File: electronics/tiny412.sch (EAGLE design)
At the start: 9 parts

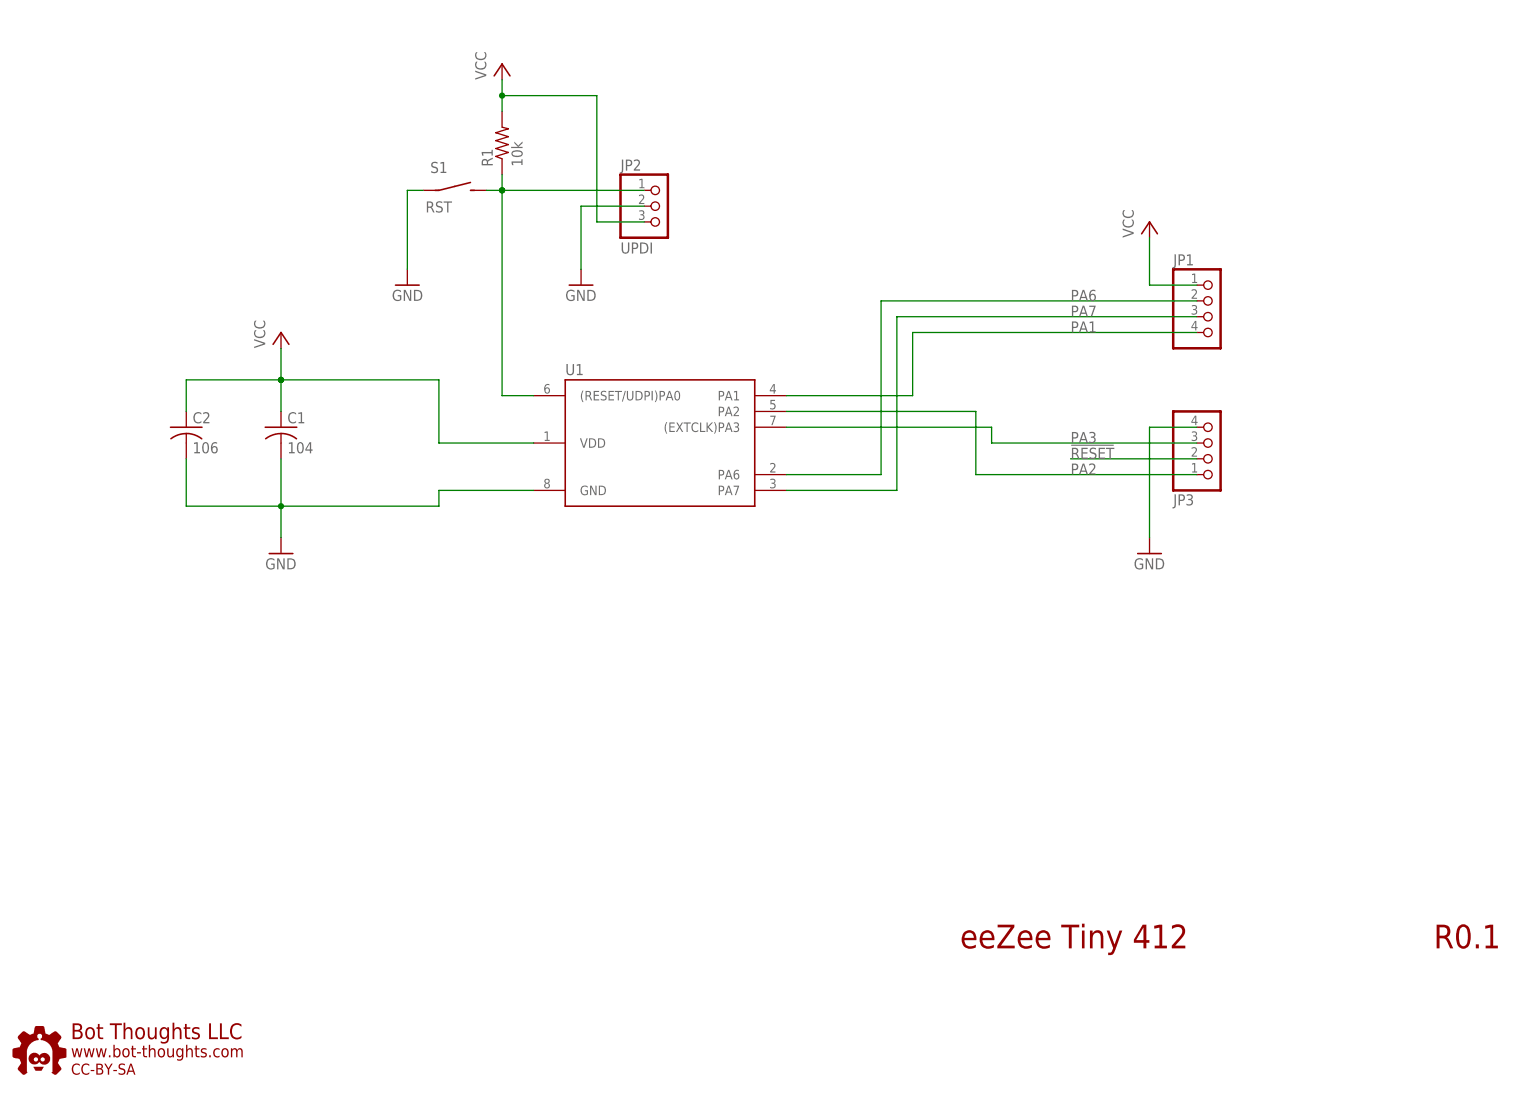
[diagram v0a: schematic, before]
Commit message: Updated silk symbols, enlarged; fixed reset ckt, added HF filter cap
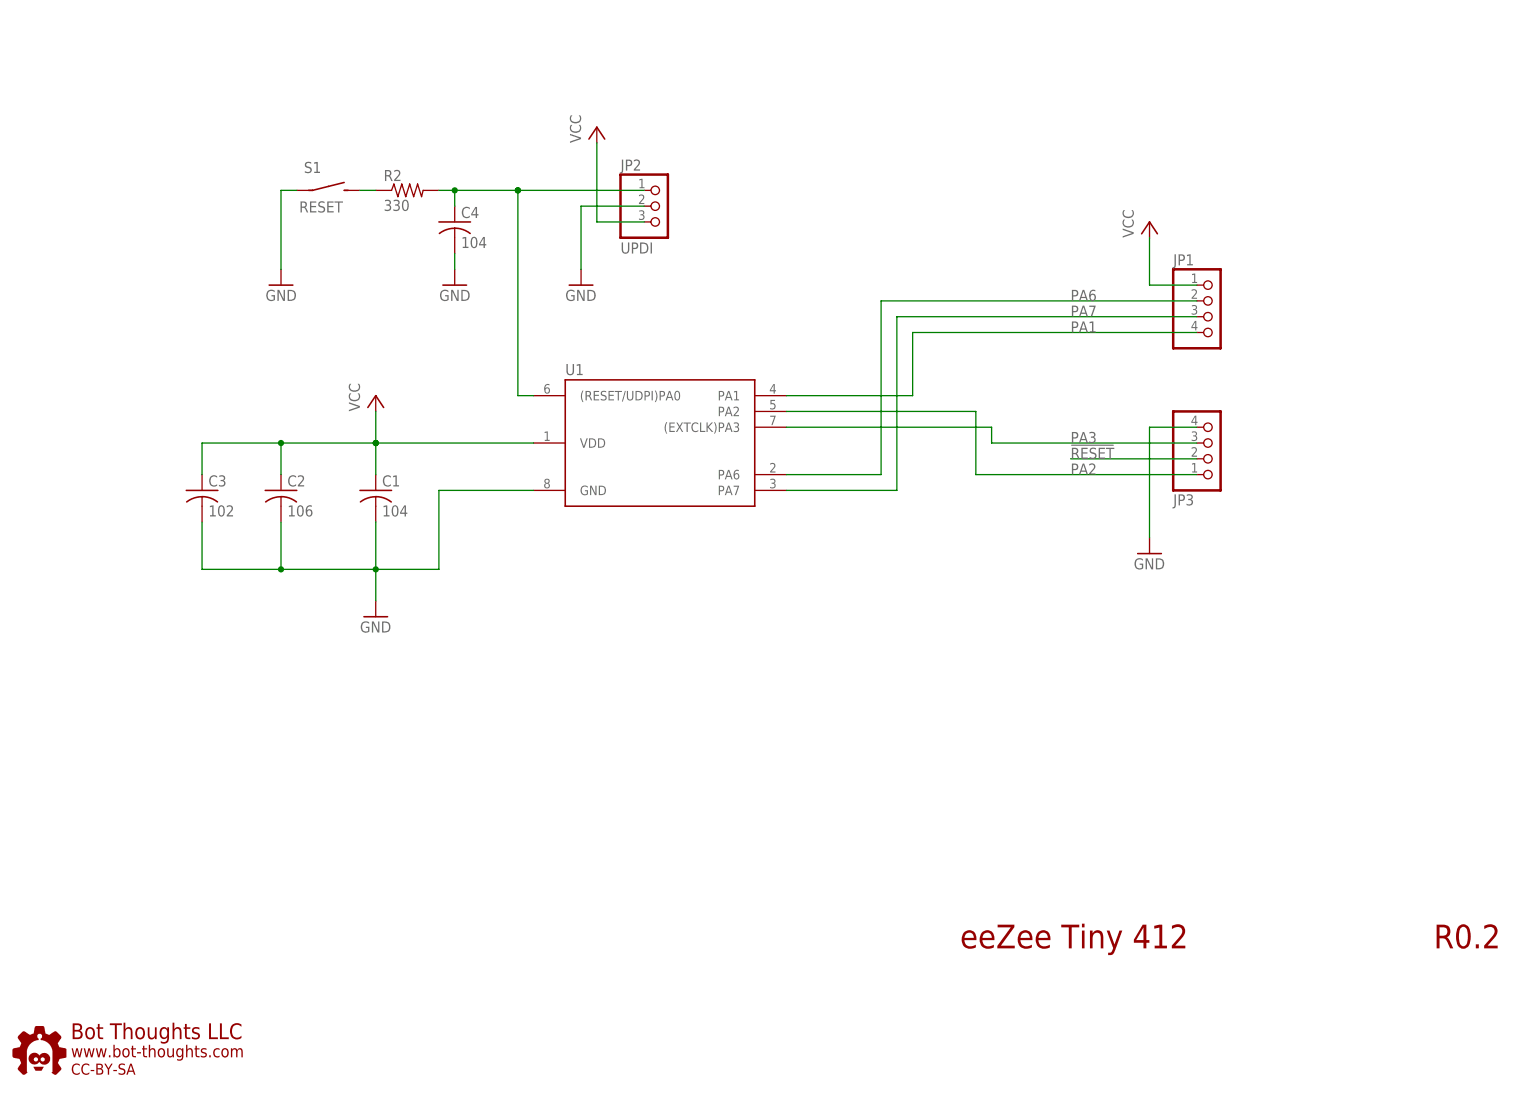
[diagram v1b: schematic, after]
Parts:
- removed R1: 10k, rcl:R-US_R0603
- added C3: 102, rcl:C-USC0603
- added C4: 104, rcl:C-USC0603
- added R2: 330, rcl:R-US_R0603
- C2: device bt_rcl:C-1206 -> bt_rcl:C-0603
- S1: value RST -> RESET
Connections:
- new net N$1: R2.1, S1.S
- net !RESET: now also C4.1, R2.2; no longer R1.1, S1.S
- net GND: now also C3.2, C4.2
- net VCC: now also C3.1; no longer R1.2
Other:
- note added: "R0.2"
- note removed: "R0.1"
- moved on the sheet: C1, C2, S1

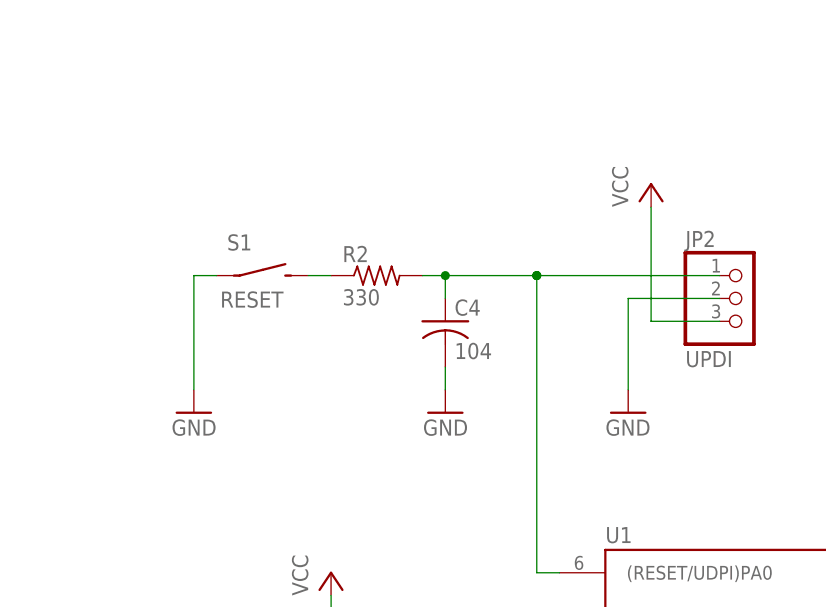
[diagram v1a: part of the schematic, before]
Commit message: remove reset, updated pin desc, added doc url
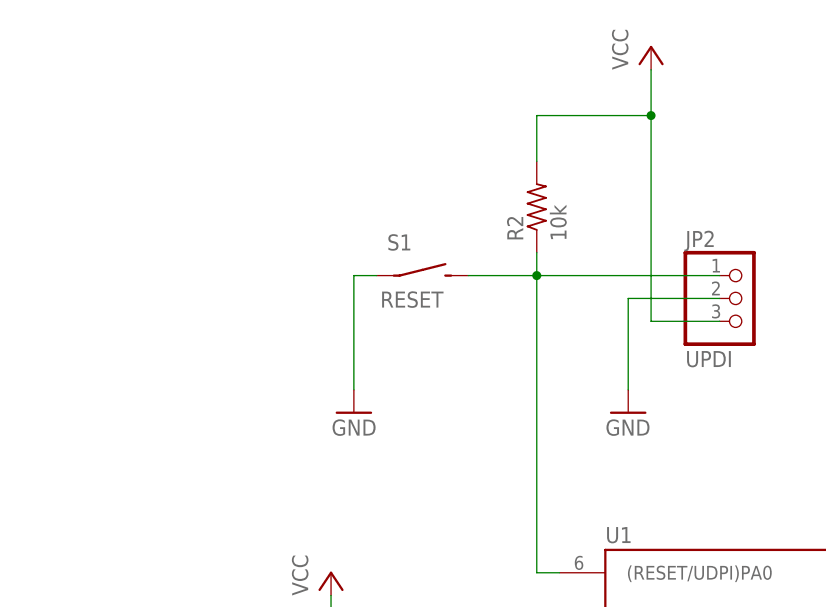
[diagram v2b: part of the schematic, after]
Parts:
- removed C4: 104, rcl:C-USC0603
- R2: value 330 -> 10k
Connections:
- removed net N$1: R2.1, S1.S
- net !RESET: now also R2.1, S1.S; no longer C4.1, R2.2
- net GND: no longer C4.2
- net VCC: now also R2.2
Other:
- moved on the sheet: R2, S1
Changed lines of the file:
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@@
 <attribute name="PARTNO" value="0603YC104KAT2A"/>
 </part>
-<part name="R2" library="rcl" deviceset="R-US_" device="R0603" value="330">
+<part name="R2" library="rcl" deviceset="R-US_" device="R0603" value="10k">
 <attribute name="PARTNO" value="ERJ-3GEYJ103V"/>
 </part>
-<part name="C4" library="rcl" deviceset="C-US" device="C0603" value="104">
-<attribute name="BOM" value="EXCLUDE"/>
-<attribute name="PARTNO" value="0603YC104KAT2A"/>
-</part>
-<part name="GND1" library="supply1" deviceset="GND" device=""/>
 </parts>
 <sheets>
@@
 </plain>
 <instances>
-<instance part="P+1" gate="VCC" x="96.52" y="154.94"/>
+<instance part="P+1" gate="VCC" x="96.52" y="170.18"/>
 <instance part="GND2" gate="1" x="93.98" y="129.54"/>
 <instance part="C1" gate="G$1" x="60.96" y="96.52">
@@
 <attribute name="BOM" value="EXCLUDE" x="60.96" y="96.52" size="1.778" layer="96" display="off"/>
 </instance>
-<instance part="GND3" gate="1" x="45.72" y="129.54" rot="MR0"/>
+<instance part="GND3" gate="1" x="63.5" y="129.54" rot="MR0"/>
 <instance part="P+2" gate="VCC" x="60.96" y="111.76"/>
 <instance part="P+4" gate="VCC" x="185.42" y="139.7"/>
@@
 </instance>
 <instance part="GND4" gate="1" x="185.42" y="86.36"/>
-<instance part="S1" gate="S1" x="53.34" y="144.78"/>
+<instance part="S1" gate="S1" x="71.12" y="144.78"/>
 <instance part="U$1" gate="G$1" x="2.54" y="2.54"/>
 <instance part="JP2" gate="A" x="106.68" y="142.24"/>
@@
 <attribute name="BOM" value="EXCLUDE" x="33.02" y="96.52" size="1.778" layer="96" display="off"/>
 </instance>
-<instance part="R2" gate="G$1" x="66.04" y="144.78">
-<attribute name="PARTNO" value="ERJ-3GEYJ103V" x="66.04" y="144.78" size="1.778" layer="96" rot="R270" display="off"/>
+<instance part="R2" gate="G$1" x="83.82" y="152.4" rot="R90">
+<attribute name="PARTNO" value="ERJ-3GEYJ103V" x="83.82" y="152.4" size="1.778" layer="96" display="off"/>
 </instance>
-<instance part="C4" gate="G$1" x="73.66" y="139.7">
-<attribute name="PARTNO" value="0603YC104KAT2A" x="73.66" y="139.7" size="1.778" layer="96" display="off"/>
-<attribute name="BOM" value="EXCLUDE" x="73.66" y="139.7" size="1.778" layer="96" display="off"/>
-</instance>
-<instance part="GND1" gate="1" x="73.66" y="129.54" rot="MR0"/>
 </instances>
 <busses>
@@
 <segment>
 <pinref part="GND3" gate="1" pin="GND"/>
-<wire x1="48.26" y1="144.78" x2="45.72" y2="144.78" width="0.1524" layer="91"/>
-<wire x1="45.72" y1="144.78" x2="45.72" y2="132.08" width="0.1524" layer="91"/>
+<wire x1="66.04" y1="144.78" x2="63.5" y2="144.78" width="0.1524" layer="91"/>
+<wire x1="63.5" y1="144.78" x2="63.5" y2="132.08" width="0.1524" layer="91"/>
 <pinref part="S1" gate="S1" pin="P"/>
 </segment>
@@
 <pinref part="GND4" gate="1" pin="GND"/>
 <pinref part="JP3" gate="A" pin="4"/>
-</segment>
-<segment>
-<pinref part="C4" gate="G$1" pin="2"/>
-<wire x1="73.66" y1="134.62" x2="73.66" y2="132.08" width="0.1524" layer="91"/>
-<pinref part="GND1" gate="1" pin="GND"/>
 </segment>
 </net>
@@
 <pinref part="JP2" gate="A" pin="3"/>
 <wire x1="104.14" y1="139.7" x2="96.52" y2="139.7" width="0.1524" layer="91"/>
-<wire x1="96.52" y1="139.7" x2="96.52" y2="152.4" width="0.1524" layer="91"/>
+<wire x1="96.52" y1="139.7" x2="96.52" y2="162.56" width="0.1524" layer="91"/>
+<pinref part="R2" gate="G$1" pin="2"/>
+<wire x1="96.52" y1="162.56" x2="96.52" y2="167.64" width="0.1524" layer="91"/>
+<wire x1="96.52" y1="162.56" x2="83.82" y2="162.56" width="0.1524" layer="91"/>
+<wire x1="83.82" y1="162.56" x2="83.82" y2="157.48" width="0.1524" layer="91"/>
+<junction x="96.52" y="162.56"/>
 </segment>
 <segment>
@@
 <net name="!RESET" class="0">
 <segment>
-<junction x="83.82" y="144.78"/>
 <wire x1="104.14" y1="144.78" x2="83.82" y2="144.78" width="0.1524" layer="91"/>
-<junction x="83.82" y="144.78"/>
-<wire x1="71.12" y1="144.78" x2="73.66" y2="144.78" width="0.1524" layer="91"/>
-<wire x1="73.66" y1="144.78" x2="83.82" y2="144.78" width="0.1524" layer="91"/>
 <wire x1="86.36" y1="111.76" x2="83.82" y2="111.76" width="0.1524" layer="91"/>
 <wire x1="83.82" y1="111.76" x2="83.82" y2="144.78" width="0.1524" layer="91"/>
 <pinref part="JP2" gate="A" pin="1"/>
 <pinref part="U1" gate="U1" pin="(RESET/UDPI)PA0"/>
-<pinref part="R2" gate="G$1" pin="2"/>
-<pinref part="C4" gate="G$1" pin="1"/>
-<wire x1="73.66" y1="142.24" x2="73.66" y2="144.78" width="0.1524" layer="91"/>
-<junction x="73.66" y="144.78"/>
+<pinref part="S1" gate="S1" pin="S"/>
+<wire x1="76.2" y1="144.78" x2="83.82" y2="144.78" width="0.1524" layer="91"/>
+<junction x="83.82" y="144.78"/>
+<pinref part="R2" gate="G$1" pin="1"/>
+<wire x1="83.82" y1="147.32" x2="83.82" y2="144.78" width="0.1524" layer="91"/>
 </segment>
 <segment>
@@
 </segment>
 </net>
-<net name="N$1" class="0">
-<segment>
-<pinref part="R2" gate="G$1" pin="1"/>
-<wire x1="58.42" y1="144.78" x2="60.96" y2="144.78" width="0.1524" layer="91"/>
-<pinref part="S1" gate="S1" pin="S"/>
-</segment>
-</net>
